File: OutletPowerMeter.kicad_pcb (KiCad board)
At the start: 2 copper layers, 170.2 x 66.3 mm, 98 parts, among them J1 TB002-500-03BE, J2 TB002V-500-03BE, J3 OLED, J4 Programmer, J5 TB002V-500-02BE, SW1 PTS647SN70SMTR2LFS, T1 115V / 9V, U1 ESP32-DEVKITC-32D, U10 ADG3304BRUZ-REEL7, U11 VX7803-500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

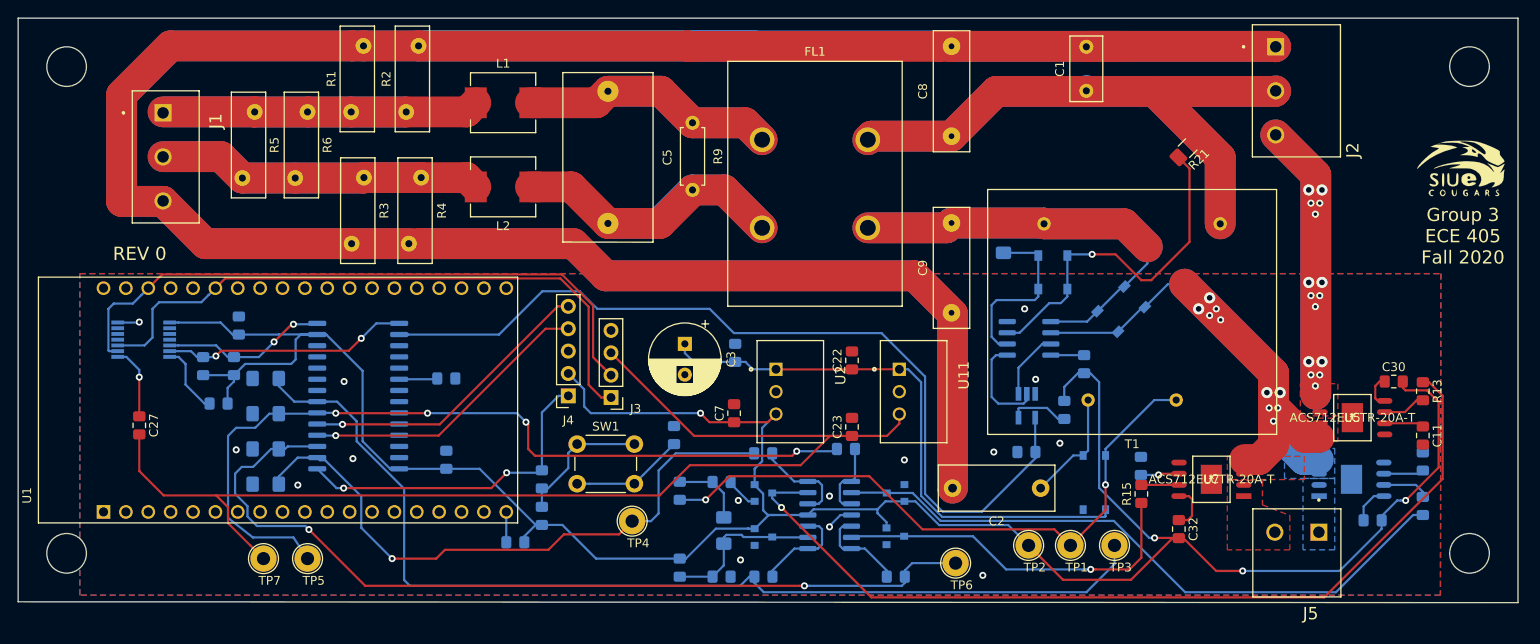
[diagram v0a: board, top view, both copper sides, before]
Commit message: Updated tactile switch and various footprints like current sensors and caps
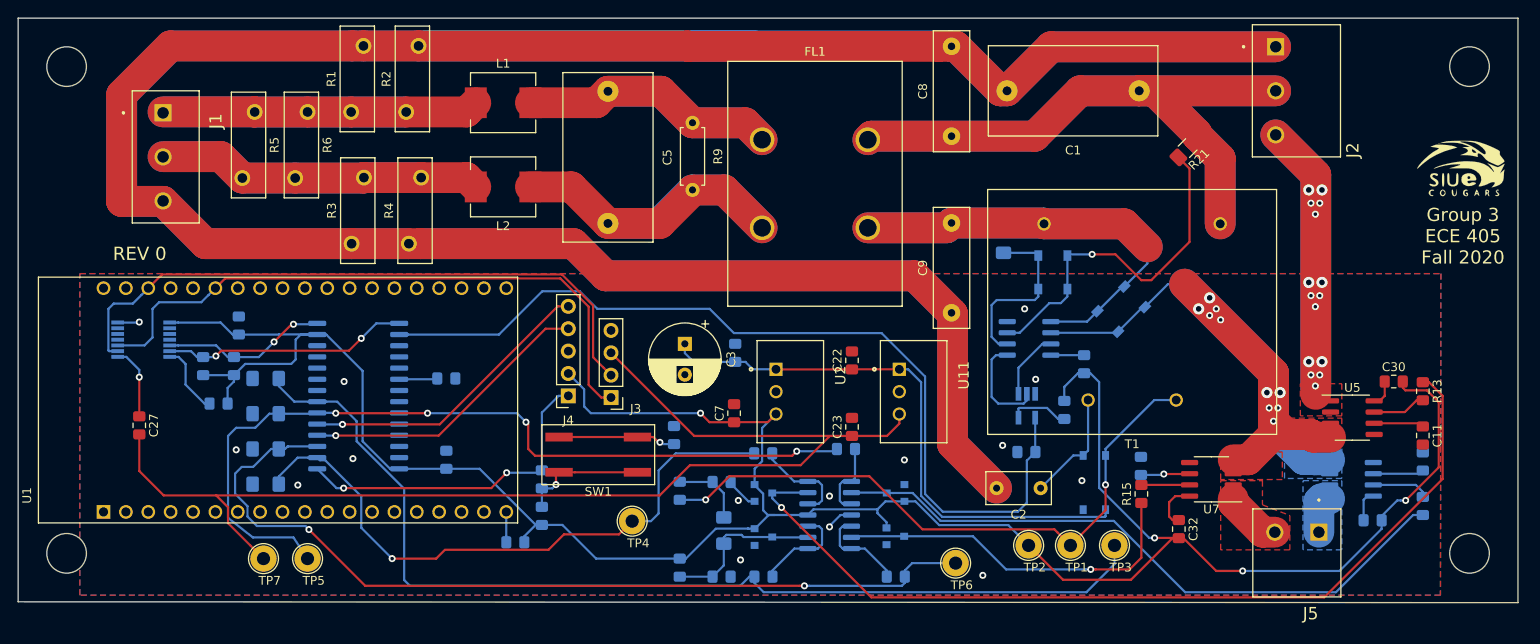
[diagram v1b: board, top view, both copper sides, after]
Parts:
- C1: footprint Capacitor_THT:C_Rect_L7.2mm_W3.5mm_P5.00mm_FKS2_FKP2_MKS2_MKP2 -> MyCustom_Footprints:C_Rect_L19.0mm_W10.0mm_P15.00mm_MKS4
- C2: footprint Capacitor_THT:C_Rect_L13.0mm_W5.0mm_P10.00mm_FKS3_FKP3_MKS4 -> Capacitor_THT:C_Rect_L7.2mm_W3.5mm_P5.00mm_FKS2_FKP2_MKS2_MKP2
- R1, R2, R3, R4, R5, R6: footprint Varistor:RV_Disc_D12mm_W3.9mm_P7.5mm -> MyCustom_Footprints:RV_Disc_D12mm_W3.9mm_P7.5mm_1.1mm
- SW1: value PTS647SN70SMTR2LFS -> KSC441GDCT70SHLFS; footprint Button_Switch_THT:SW_PUSH_6mm_H5mm -> MyCustom_Footprints:KSC4
- U5, U6, U7: footprint MyCustom_Footprints:ACS712ELCTR-30A-T -> Package_SO:SOIC-8_3.9x4.9mm_P1.27mm
- moved C1 6.00 mm to (190.0, 80.5), turned to 180 degrees
- moved SW1 2.68 mm to (128.6, 121.8)
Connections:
- SW1 pad 1: Net-(R22-Pad2) -> Net-(C18-Pad1)
- SW1 pad 2: Net-(C18-Pad1) -> Net-(R22-Pad2)
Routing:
- net EARTH: track 570.4 -> 578.4 mm
- net NEUTRAL_OUT: track 81.5 -> 88.2 mm
- net NEUT_3: track 0.00 -> 6.55 mm
- net NEUT_2: track 0.00 -> 4.84 mm
- net PF_OUT: track 99.6 -> 101.9 mm
- net Net-(C31-Pad1): track 5.14 -> 3.60 mm
- net HOT_OUT: track 133.7 -> 135.1 mm
- net Net-(R22-Pad2): track 15.7 -> 14.3 mm, vias 0 -> 1
- net Net-(R14-Pad2): track 5.33 -> 6.53 mm
- net Net-(C12-Pad1): track 4.58 -> 5.78 mm
- net Net-(R15-Pad2): track 4.28 -> 5.47 mm
- net Net-(R13-Pad2): track 4.88 -> 6.08 mm
- net Net-(C13-Pad1): track 4.38 -> 5.58 mm
- net Net-(C11-Pad1): track 4.48 -> 5.68 mm
- net NEUT_1: track 62.7 -> 61.7 mm
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
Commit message: Added tactile switch model. Resized ground planes and more via stitching
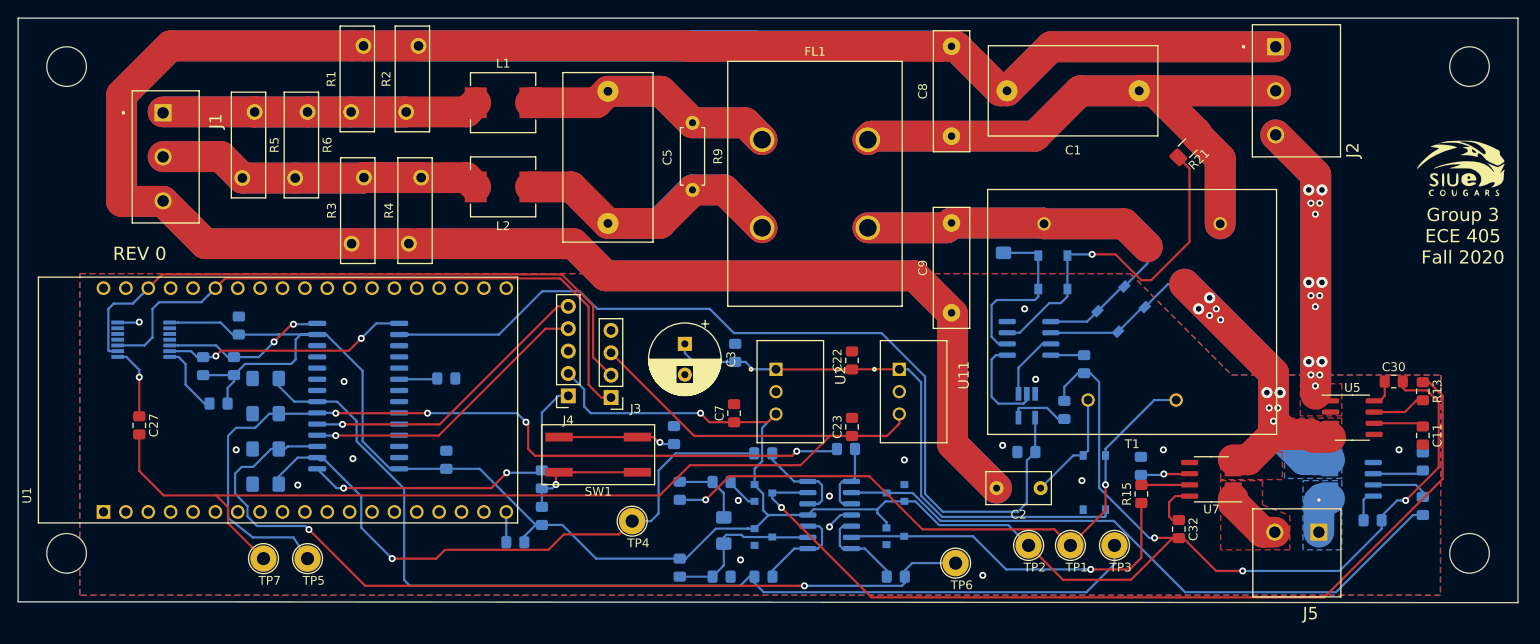
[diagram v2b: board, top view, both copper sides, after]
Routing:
- net GND: vias 15 -> 17
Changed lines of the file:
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@@
     (thickness 1.6)
     (drawings 7)
-    (tracks 726)
+    (tracks 728)
     (zones 0)
     (modules 98)
@@
     (pad 1 smd rect (at -4.45 -2) (size 3.1 1) (layers F.Cu F.Paste F.Mask)
       (net 83 "Net-(C18-Pad1)"))
+    (model "${KIPRJMOD}/Models.3dshapes/KSC441G DCT_cp.stp"
+      (at (xyz 0 0 0))
+      (scale (xyz 1 1 1))
+      (rotate (xyz 0 0 0))
+    )
   )
   (module Capacitor_THT:C_Rect_L7.2mm_W3.5mm_P5.00mm_FKS2_FKP2_MKS2_MKP2 (layer F.Cu)
@@
     (pad 2 thru_hole circle (at 0 10) (size 2.8 2.8) (drill 2) (layers *.Cu *.Mask)
       (net 6 "Net-(C5-Pad2)"))
-    (model ${KISYS3DMOD}/Inductor_THT.3dshapes/L_CommonMode_Wuerth_WE-CMB-L.wrl
-      (at (xyz 0 0 0))
-      (scale (xyz 1 1 1))
-      (rotate (xyz 0 0 0))
-    )
     (model ${KIPRJMOD}/Models.3dshapes/S14100038_cp.step
       (at (xyz 0 0 0))
@@
     (pad 2 smd rect (at 3.1 0 180) (size 2.5 3.5) (layers F.Cu F.Paste F.Mask)
       (net 22 NEUTRAL))
-    (model ${KISYS3DMOD}/Inductor_SMD.3dshapes/L_7.3x7.3_H3.5.wrl
-      (at (xyz 0 0 0))
-      (scale (xyz 1 1 1))
-      (rotate (xyz 0 0 0))
-    )
     (model ${KIPRJMOD}/Models.3dshapes/MGV0603R33M-10.step
       (at (xyz 0 0 0))
@@
     (pad 2 smd rect (at 3.1 0) (size 2.5 3.5) (layers F.Cu F.Paste F.Mask)
       (net 5 "Net-(C5-Pad1)"))
-    (model ${KISYS3DMOD}/Inductor_SMD.3dshapes/L_7.3x7.3_H3.5.wrl
-      (at (xyz 0 0 0))
-      (scale (xyz 1 1 1))
-      (rotate (xyz 0 0 0))
-    )
     (model ${KIPRJMOD}/Models.3dshapes/MGV0603R33M-10.step
       (at (xyz 0 0 0))
@@
   (segment (start 154.75 130) (end 156.1 128.65) (width 0.25) (layer B.Cu) (net 4))
   (via (at 144.5 127) (size 0.8) (drill 0.4) (layers F.Cu B.Cu) (net 4))
+  (via (at 192.75 121.25) (size 0.8) (drill 0.4) (layers F.Cu B.Cu) (net 4))
+  (via (at 219.5 121.25) (size 0.8) (drill 0.4) (layers F.Cu B.Cu) (net 4))
   (segment (start 135.72 80.55) (end 139.3 84.13) (width 3.5) (layer F.Cu) (net 5))
   (segment (start 129.7 80.55) (end 135.72 80.55) (width 3.5) (layer F.Cu) (net 5))
@@
     (polygon
       (pts
-        (xy 224.2 137.75) (xy 69.75 137.75) (xy 69.75 101.25) (xy 224.25 101.25)
+        (xy 224.2 137.75) (xy 69.75 137.75) (xy 69.75 101.25) (xy 189 101.25) (xy 200.5 112.75)
+        (xy 224.25 112.75)
       )
     )
@@
     (polygon
       (pts
-        (xy 224.2 137.75) (xy 69.75 137.75) (xy 69.75 101.25) (xy 224.25 101.25)
+        (xy 224.2 137.75) (xy 69.75 137.75) (xy 69.75 101.25) (xy 189 101.25) (xy 200.5 112.75)
+        (xy 224.25 112.773748)
       )
     )

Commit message: Fixed Vcc capacitors. Added more vias.
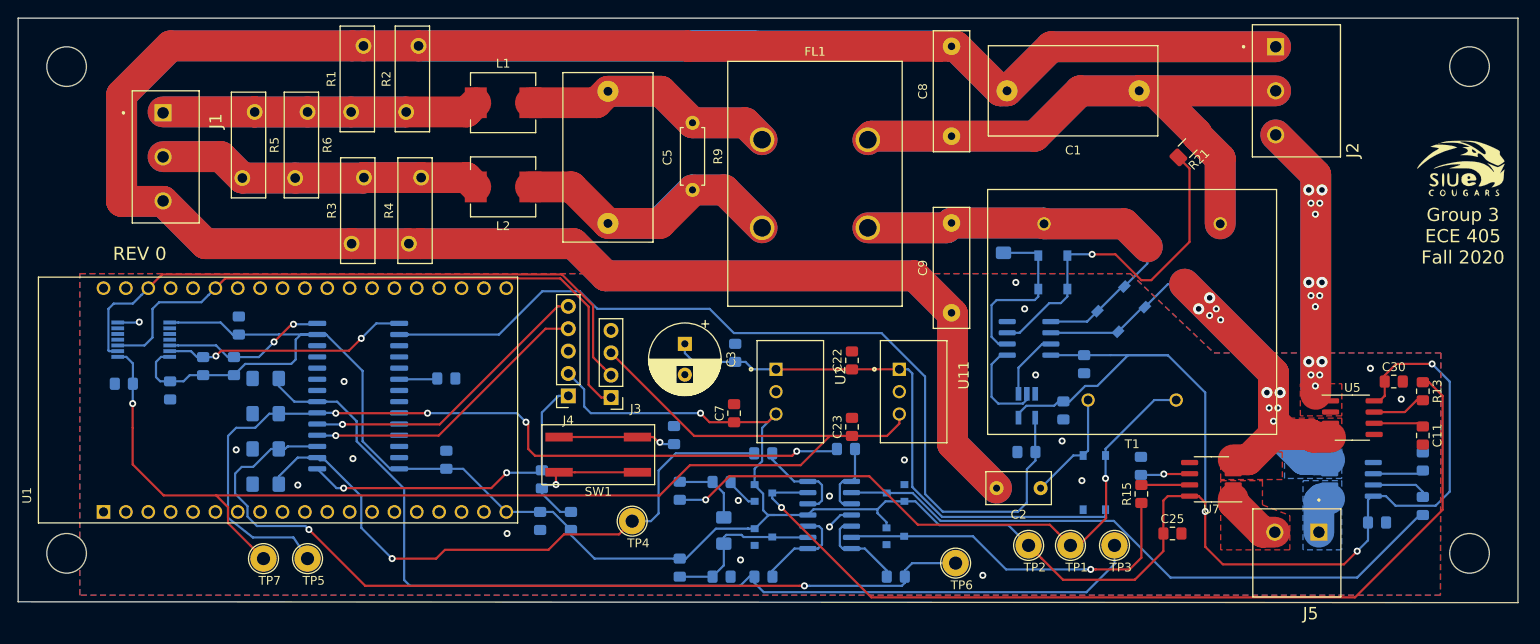
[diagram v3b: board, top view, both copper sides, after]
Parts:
- removed C32: 0.1uF, Capacitor_SMD:C_0805_2012Metric_Pad1.15x1.40mm_HandSolder
- added C25: 0.1uF, Capacitor_SMD:C_0805_2012Metric_Pad1.15x1.40mm_HandSolder, F.Cu at (193.8, 130.8)
- C27: moved to B.Cu
- moved C29 5.70 mm to (80.0, 114.5), turned to 270 degrees
- moved C27 5.04 mm to (74.8, 113.8), turned to 0 degrees
- moved C24 3.72 mm to (122.0, 129.3), turned to 270 degrees
- moved R25 3.35 mm to (125.5, 129.3)
- moved C31 0.56 mm to (217.0, 129.5)
- moved C26 0.11 mm to (181.4, 116.8)
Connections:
- C24 pad 1: Net-(C24-Pad1) -> VCC
- C24 pad 2: VCC -> GND
- C26 pad 2: Net-(C26-Pad2) -> GND
- C27 pad 1: Net-(C27-Pad1) -> GND
- C28 pad 1: Net-(C28-Pad1) -> VCC
- C28 pad 2: VCC -> GND
- C29 pad 2: Net-(C29-Pad2) -> GND
- C30 pad 1: Net-(C30-Pad1) -> VCC
- C30 pad 2: VCC -> GND
- C31 pad 1: Net-(C31-Pad1) -> VCC
- C31 pad 2: VCC -> GND
- U1 pad 19: Net-(C24-Pad1) -> VCC
- U10 pad 1: Net-(C27-Pad1) -> 3V3
- U10 pad 14: Net-(C29-Pad2) -> VCC
- U5 pad 8: Net-(C30-Pad1) -> VCC
- U6 pad 8: Net-(C31-Pad1) -> VCC
- U7 pad 8: Net-(C32-Pad1) -> VCC
- U8 pad 8: Net-(C28-Pad1) -> VCC
- U9 pad 5: Net-(C26-Pad2) -> VCC
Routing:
- net VCC: track 284.4 -> 336.3 mm
- net 3V3: track 134.2 -> 144.6 mm, vias 0 -> 1
- net Net-(C27-Pad1): track 8.34 -> 0.00 mm, vias 1 -> 0
- net Net-(C29-Pad2): track 8.10 -> 0.00 mm
- net Net-(C26-Pad2): track 6.78 -> 0.00 mm
- net Net-(C32-Pad1): track 5.50 -> 0.00 mm
- net Net-(C28-Pad1): track 3.78 -> 0.00 mm
- net Net-(C31-Pad1): track 3.60 -> 0.00 mm
- net Net-(C24-Pad1): track 3.45 -> 0.00 mm
- net Net-(C30-Pad1): track 3.06 -> 0.00 mm
- net Net-(R22-Pad2): track 14.3 -> 17.0 mm
- net Net-(D3-Pad3): track 103.3 -> 105.3 mm
- net Net-(D4-Pad3): track 73.2 -> 71.8 mm
- net 9V: track 71.6 -> 72.2 mm
- net GND: vias 17 -> 19

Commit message: Changed capacitor footprint to 1210 as well as the symbol.
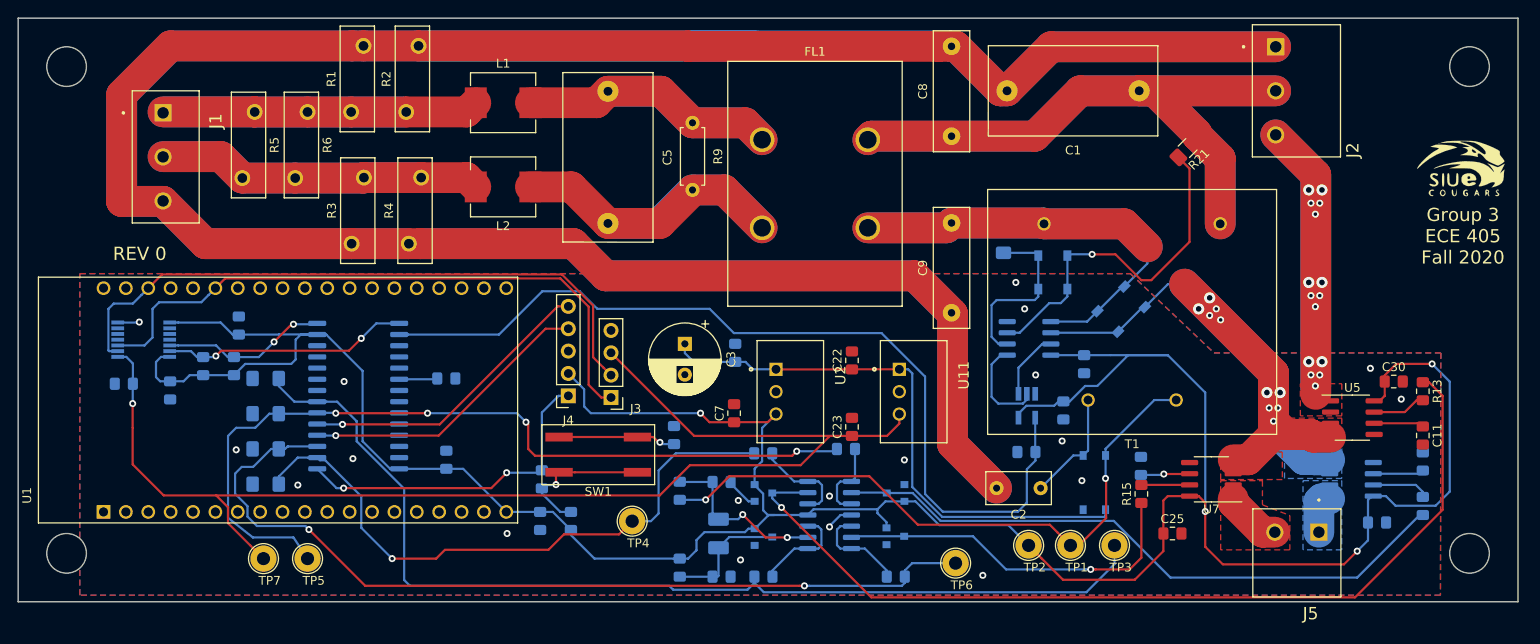
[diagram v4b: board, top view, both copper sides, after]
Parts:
- C6: footprint Capacitor_SMD:C_1206_3216Metric_Pad1.42x1.75mm_HandSolder -> Capacitor_Tantalum_SMD:CP_EIA-3528-21_Kemet-B_Pad1.50x2.35mm_HandSolder
- moved C6 0.69 mm to (142.2, 130.8), turned to 270 degrees
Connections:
- D2 pad 3: Net-(C6-Pad1) -> Net-(C6-Pad2)
- R10 pad 2: Net-(C6-Pad1) -> Net-(C6-Pad2)
- R11 pad 1: Net-(C6-Pad1) -> Net-(C6-Pad2)
- R7 pad 2: Net-(C6-Pad2) -> Net-(C6-Pad1)
- R8 pad 1: Net-(C6-Pad2) -> Net-(C6-Pad1)
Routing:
- net Net-(C6-Pad2): track 8.25 -> 14.2 mm
- net Net-(C6-Pad1): track 18.5 -> 19.6 mm, vias 0 -> 2
- net Net-(R18-Pad2): track 10.5 -> 11.1 mm
- net Net-(R17-Pad2): track 8.61 -> 9.19 mm
- net VCC: track 336.3 -> 336.8 mm
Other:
- board size 170.2 x 66.3 mm -> 170.2 x 66.2 mm

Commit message: Revision 1 completed. Order sent to JLCPCB. Routed traces, rearranged components, and changed footprints.
	new file:   Gerber.zip
	modified:   OutletPowerMeter.kicad_pcb
	modified:   OutletPowerMeter.kicad_pcb-bak
	modified:   OutletPowerMeter.net
	modified:   OutletPowerMeter.sch
	modified:   OutletPowerMeter.sch-bak
	modified:   OutletPowerMeter.xml
	modified:   OutletPowerMeter.zip
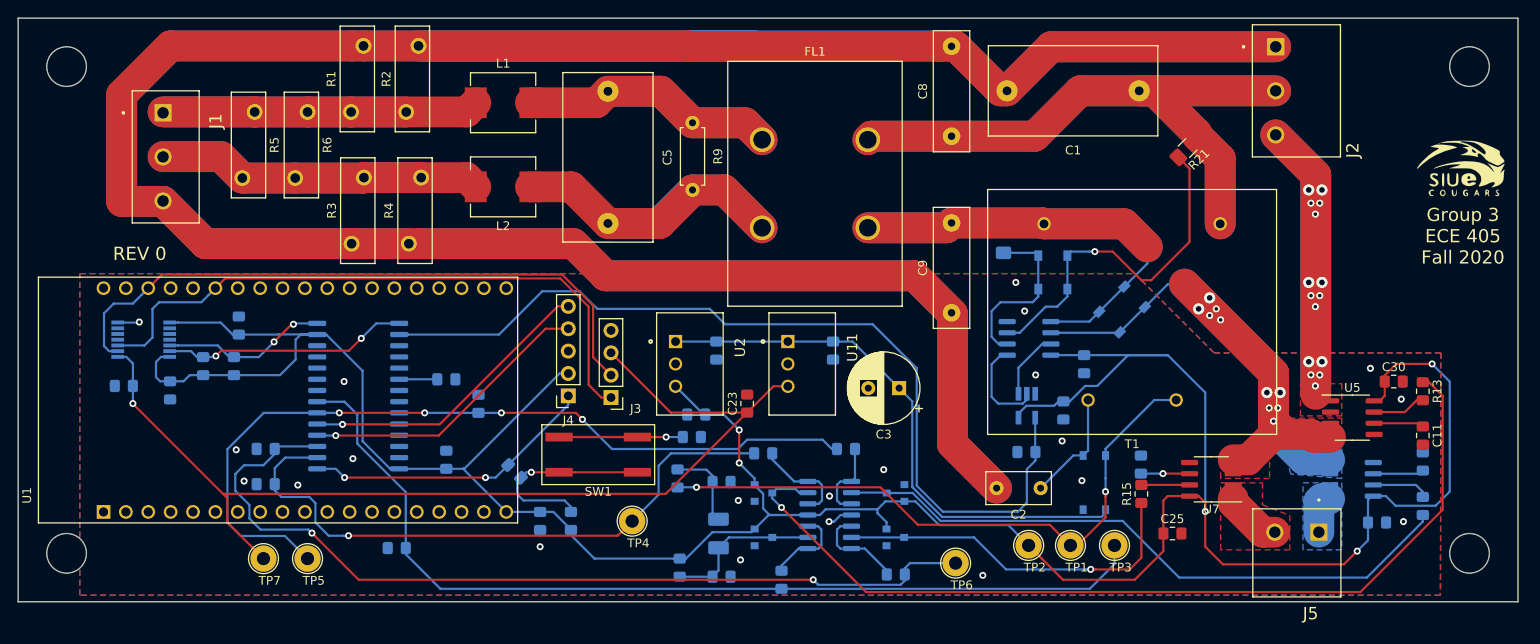
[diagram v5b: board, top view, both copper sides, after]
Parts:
- C10, C14, C15, C16: footprint Capacitor_SMD:C_1206_3216Metric_Pad1.42x1.75mm_HandSolder -> Capacitor_SMD:C_0805_2012Metric_Pad1.15x1.40mm_HandSolder
- C22, C7: moved to B.Cu
- moved C3 24.8 mm to (162.8, 114.2), turned to 180 degrees
- moved C10 24.3 mm to (105.7, 132.4)
- moved C15 24.2 mm to (115.0, 116.0), turned to 90 degrees
- moved U11 13.0 mm to (151.8, 111.5)
- moved C23 12.2 mm to (145.5, 116.0)
- moved U2 11.8 mm to (139.0, 111.5)
- moved C7 4.30 mm to (139.7, 117.2), turned to 180 degrees
- moved R22 3.23 mm to (119.1, 123.7), turned to 315 degrees
- moved C22 2.42 mm to (155.2, 110.0), turned to 270 degrees
- moved C4 2.16 mm to (142.0, 110.0), turned to 270 degrees
- moved R12 2.08 mm to (149.4, 136.0), turned to 90 degrees
- moved C18 2.04 mm to (139.2, 119.8), turned to 0 degrees
- moved R7 1.42 mm to (137.6, 124.5)
- moved C27 0.25 mm to (74.8, 114.0)
- moved R18 0.25 mm to (162.4, 135.4)
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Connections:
- U3 pad 2: Net-(C6-Pad1) -> Net-(C6-Pad2)
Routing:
- net 3V3: track 144.6 -> 117.8 mm
- net Net-(C6-Pad1): track 19.6 -> 9.47 mm, vias 2 -> 0
- net V_SENSOR: track 117.6 -> 108.6 mm
- net Net-(R22-Pad2): track 17.0 -> 22.8 mm
- net MCLR: track 37.6 -> 33.4 mm
- net VCC: track 336.8 -> 332.7 mm, vias 4 -> 5
- net GND: track 9.36 -> 5.32 mm, vias 19 -> 21
- net Net-(C6-Pad2): track 14.2 -> 17.9 mm
- net CURR_2: track 94.6 -> 92.6 mm
- net Net-(C22-Pad1): track 64.9 -> 63.3 mm
- net 9V: track 72.2 -> 70.7 mm
- net Net-(R12-Pad2): track 10.9 -> 9.55 mm
- net CURR_1: track 70.4 -> 71.5 mm
- net Net-(C18-Pad1): track 13.4 -> 14.1 mm
